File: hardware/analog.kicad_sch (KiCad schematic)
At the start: 27 parts, among them J3 73101-0570, U13 TLP3441TP_F, U14 ${SIM.PARAMS}, U15 ADG621BRMZ, U16 ${SIM.PARAMS}, U18 ${SIM.PARAMS}

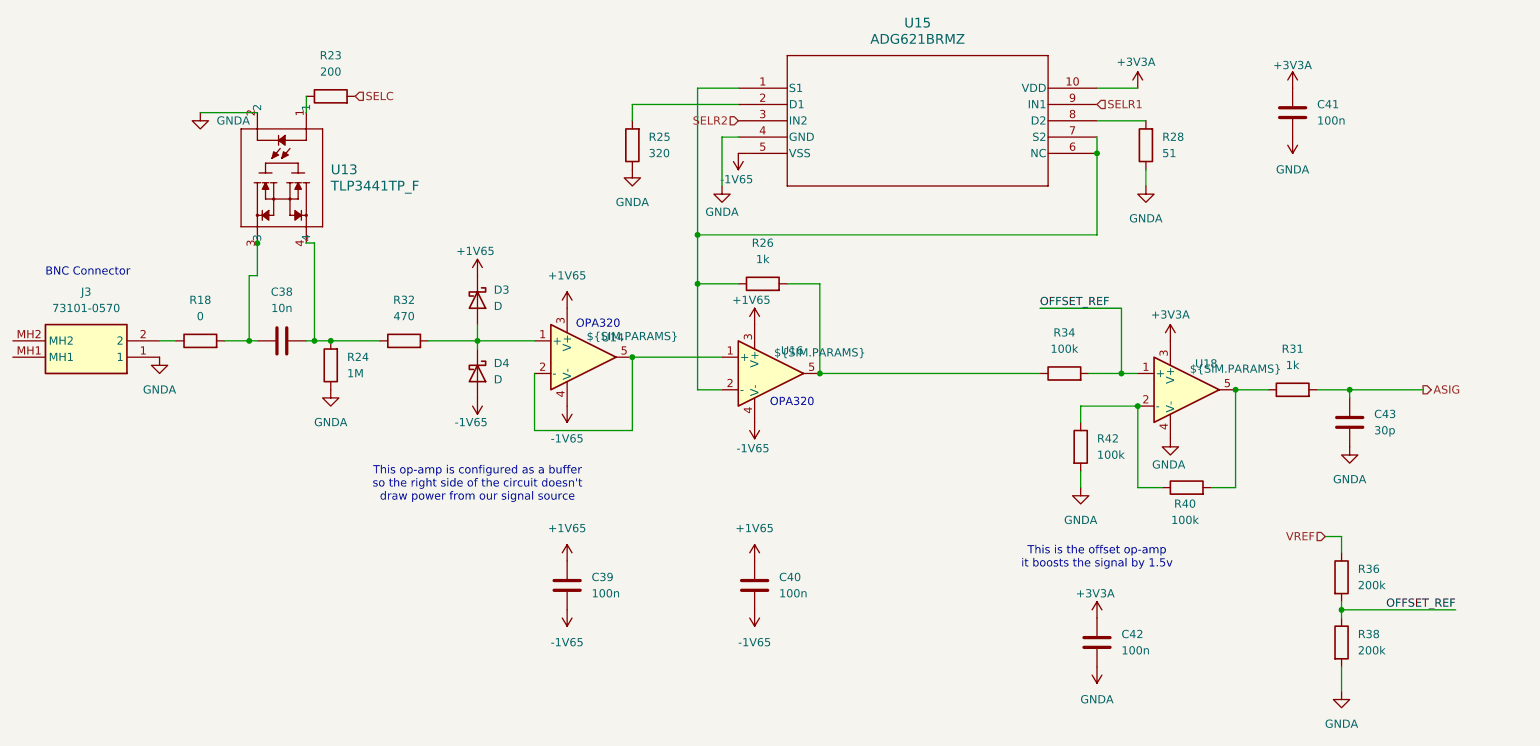
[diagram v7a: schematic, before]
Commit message: feat(hardware): Add test point connections + update PCB layout
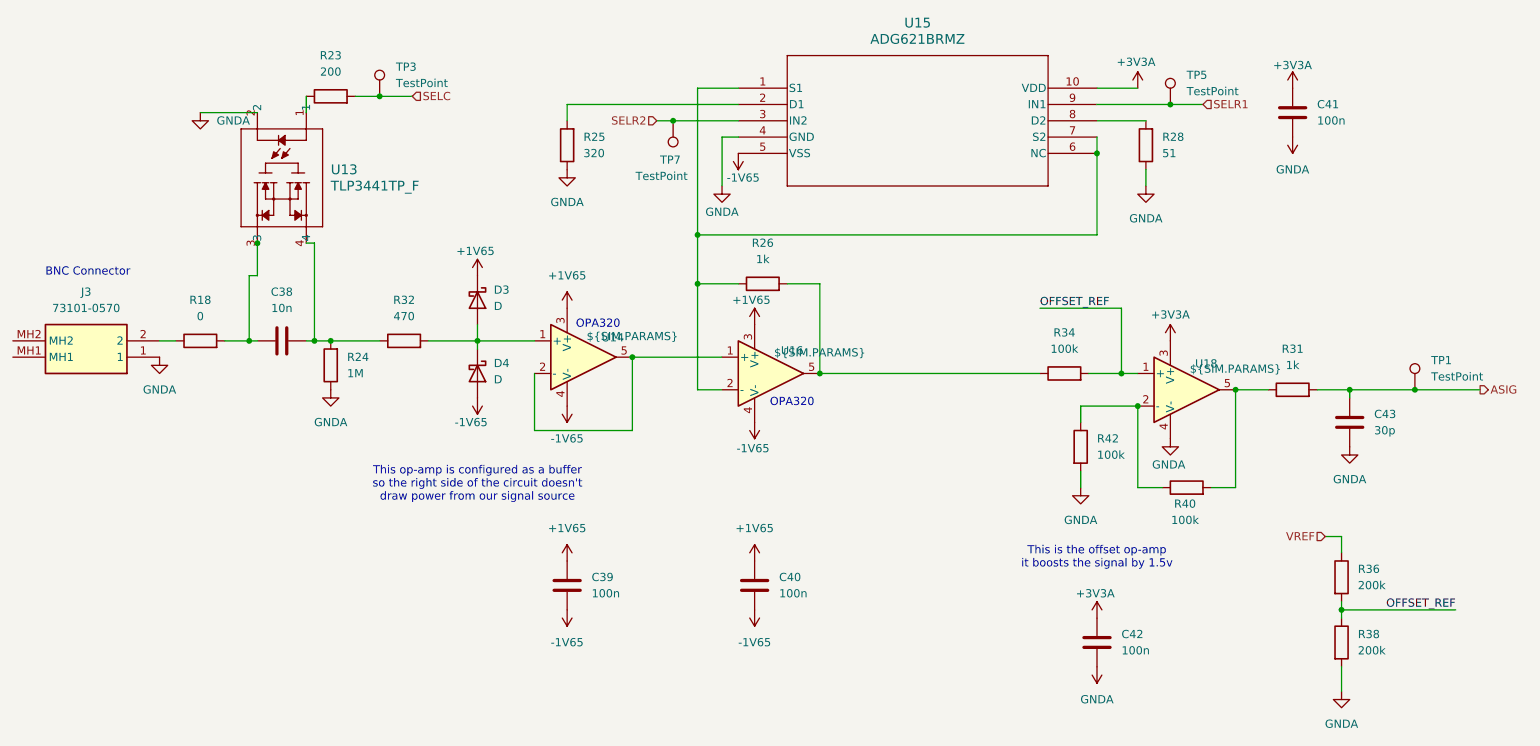
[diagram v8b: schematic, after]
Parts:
- added TP1, TP3, TP5, TP7: TestPoint, CustomTestPoints:TestPoint_0603_1608Metric, symbol Connector:TestPoint
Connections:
- net ASIG: now also TP1.1
- net SELC: now also TP3.1
- net SELR1: now also TP5.1
- net SELR2: now also TP7.1
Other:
- moved on the sheet: R25
